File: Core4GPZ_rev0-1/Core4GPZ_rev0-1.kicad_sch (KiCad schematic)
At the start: 4 parts, among them U2 core4, U3 MPXHZ6250AC6T1

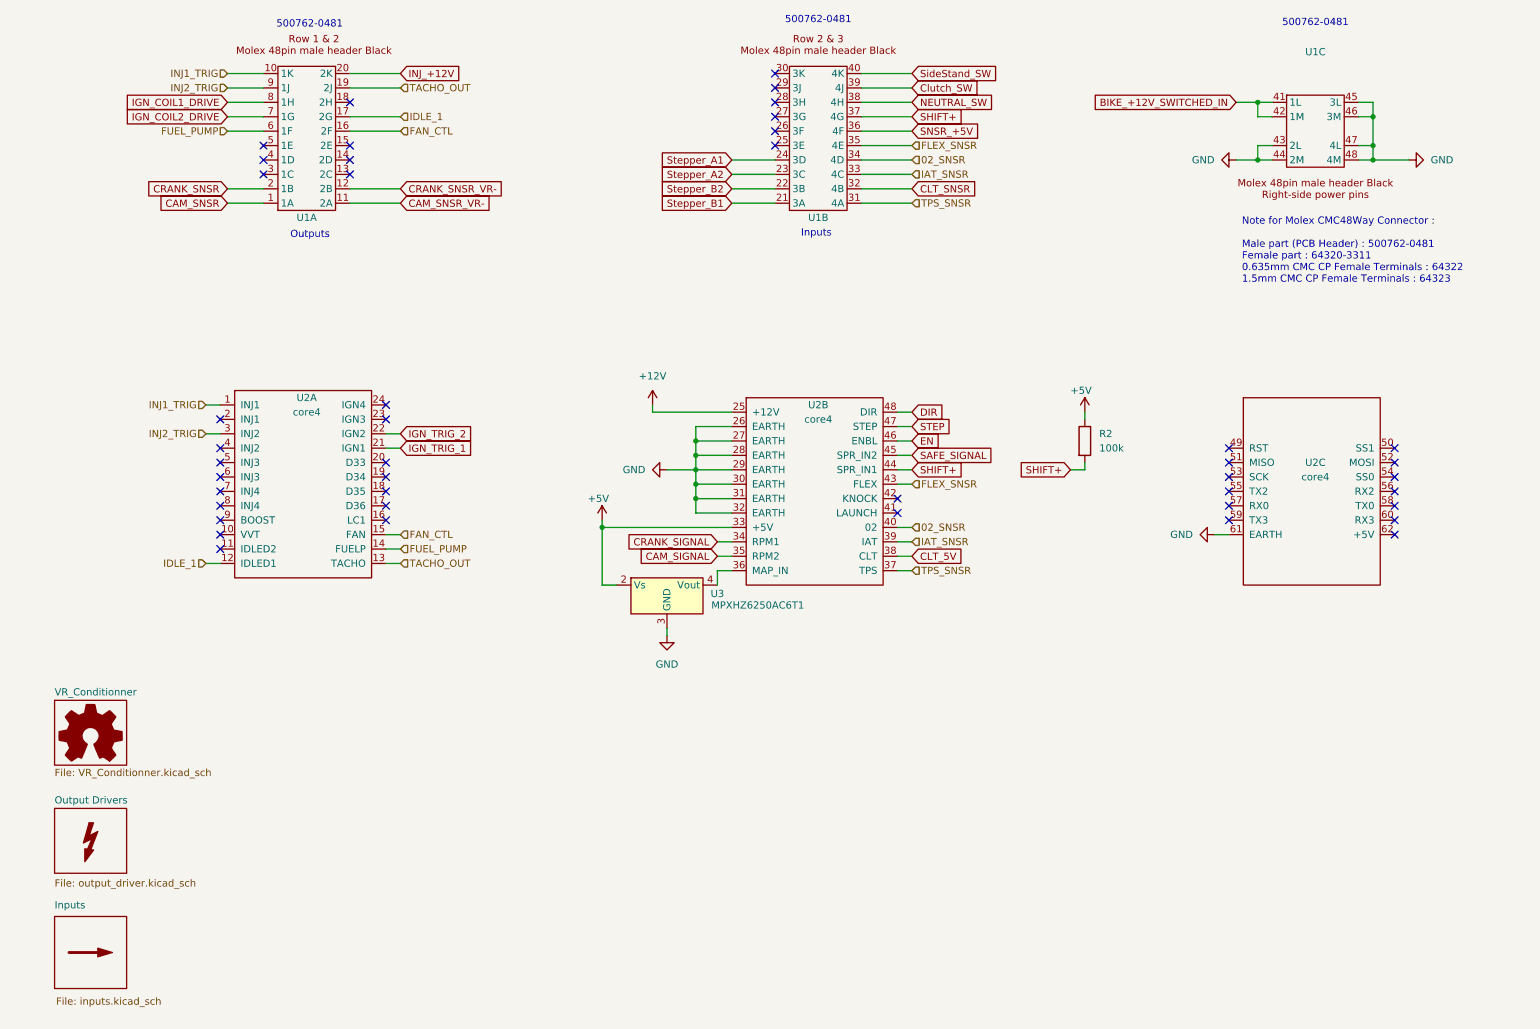
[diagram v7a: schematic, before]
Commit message: Updated component Library with specific parts
Added "Speeduino_bike_prototype" library, with symbols and footprints.
You can add this library to your library table.
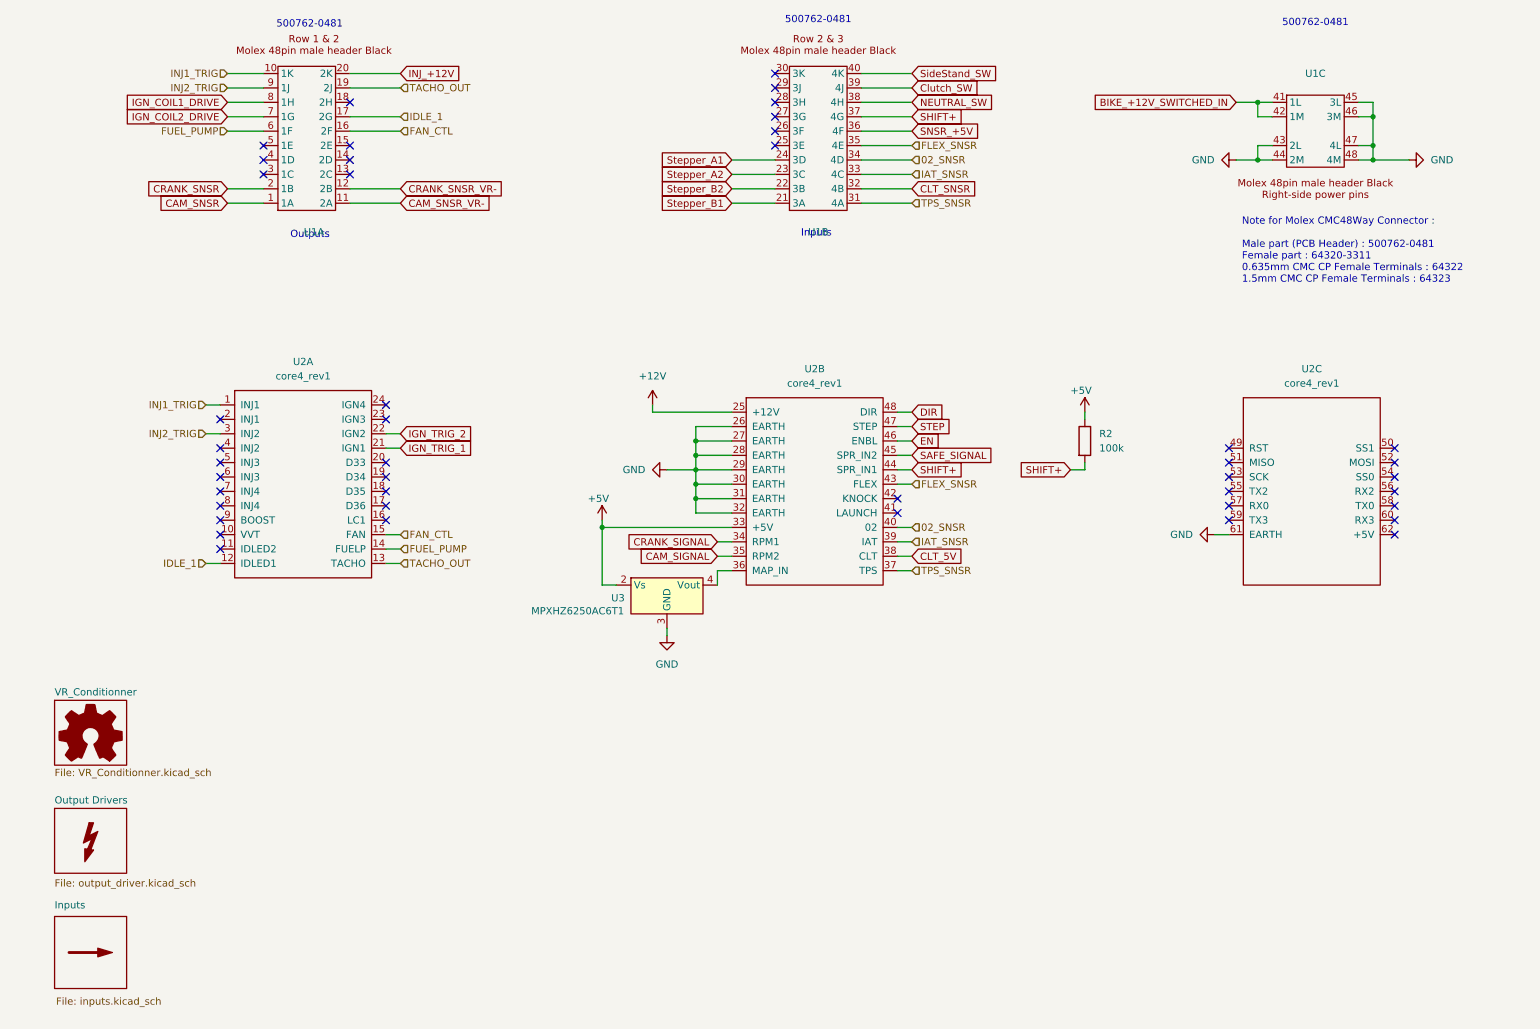
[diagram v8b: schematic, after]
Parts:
- removed U1: ~, Molex_CMC_Conn:Molex_CMC_48pin_Male_Black, symbol Molex_CMC_Conn:Molex_Conn_48_Male_Black
- removed U2: core4, CORE4:Core4_rev1, symbol Core4:core4
- removed U3: MPXHZ6250AC6T1, IC_Automotive:MPXHZ6250AC6T1, symbol Speeduino_Misc:MPXHZ6250AC6T1
- added U1: ~, Speeduino_Bike_Prototype:Molex_CMC_48pin_Male_Black, symbol Speeduino_Bike_Prototype:Molex_Conn_48_Male_Black
- added U2: core4_rev1, Speeduino_Bike_Prototype:Core4, symbol Speeduino_Bike_Prototype:core4_rev1
- added U3: MPXHZ6250AC6T1, Speeduino_Bike_Prototype:MPXHZ6250AC6T1, symbol Speeduino_Bike_Prototype:MPXHZ6250AC6T1
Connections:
- net +12V: now also U2.25 (+12V)
- net +5V: now also U2.33 (+5V), U3.2 (Vs)
- net 02_SNSR: now also U1.34 (4D), U2.40 (02)
- net BIKE_+12V_SWITCHED_IN: now also U1.41 (1L), U1.42 (1M)
- net CAM_SIGNAL: now also U2.35 (RPM2)
- net CAM_SNSR: now also U1.1 (1A)
- net CAM_SNSR_VR-: now also U1.11 (2A)
- net CLT_5V: now also U2.38 (CLT)
- net CLT_SNSR: now also U1.32 (4B)
- net CRANK_SIGNAL: now also U2.34 (RPM1)
- net CRANK_SNSR: now also U1.2 (1B)
- net CRANK_SNSR_VR-: now also U1.12 (2B)
- net Clutch_SW: now also U1.39 (4J)
- net DIR: now also U2.48 (DIR)
- net EN: now also U2.46 (ENBL)
- net FAN_CTL: now also U1.16 (2F), U2.15 (FAN)
- net FLEX_SNSR: now also U1.35 (4E), U2.43 (FLEX)
- net FUEL_PUMP: now also U1.6 (1F), U2.14 (FUELP)
- net GND: now also U1.43 (2L), U1.44 (2M), U1.45 (3L), U1.46 (3M), U1.47 (4L), U1.48 (4M), U2.26 (EARTH), U2.27 (EARTH), U2.28 (EARTH), U2.29 (EARTH), U2.30 (EARTH), U2.31 (EARTH), U2.32 (EARTH), U2.61 (EARTH), U3.3 (GND)
- net IAT_SNSR: now also U1.33 (4C), U2.39 (IAT)
- net IDLE_1: now also U1.17 (2G), U2.12 (IDLED1)
- net IGN_COIL1_DRIVE: now also U1.8 (1H)
- net IGN_COIL2_DRIVE: now also U1.7 (1G)
- net IGN_TRIG_1: now also U2.21 (IGN1)
- net IGN_TRIG_2: now also U2.22 (IGN2)
- net INJ1_TRIG: now also U1.10 (1K), U2.1 (INJ1)
- net INJ2_TRIG: now also U1.9 (1J), U2.3 (INJ2)
- net INJ_+12V: now also U1.20 (2K)
- net NEUTRAL_SW: now also U1.38 (4H)
- net SAFE_SIGNAL: now also U2.45 (SPR_IN2)
- net SHIFT+: now also U1.37 (4G), U2.44 (SPR_IN1)
- net SNSR_+5V: now also U1.36 (4F)
- net STEP: now also U2.47 (STEP)
- net SideStand_SW: now also U1.40 (4K)
- net Stepper_A1: now also U1.24 (3D)
- net Stepper_A2: now also U1.23 (3C)
- net Stepper_B1: now also U1.21 (3A)
- net Stepper_B2: now also U1.22 (3B)
- net TACHO_OUT: now also U1.19 (2J), U2.13 (TACHO)
- net TPS_SNSR: now also U1.31 (4A), U2.37 (TPS)
- new net: U2.36 (MAP_IN), U3.4 (Vout)
